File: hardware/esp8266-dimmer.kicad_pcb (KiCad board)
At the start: 2 copper layers, 68.5 x 26 mm, 18 parts, among them J1 Conn_01x06, J2 Conn_01x05, J3 Screw_Terminal_01x02, Q1 PMV16XN, Q2 PMV16XN, Q3 PMV16XN, Q4 PMV16XN, U1 LD1117S33TR_SOT223, U2 ESP-12E

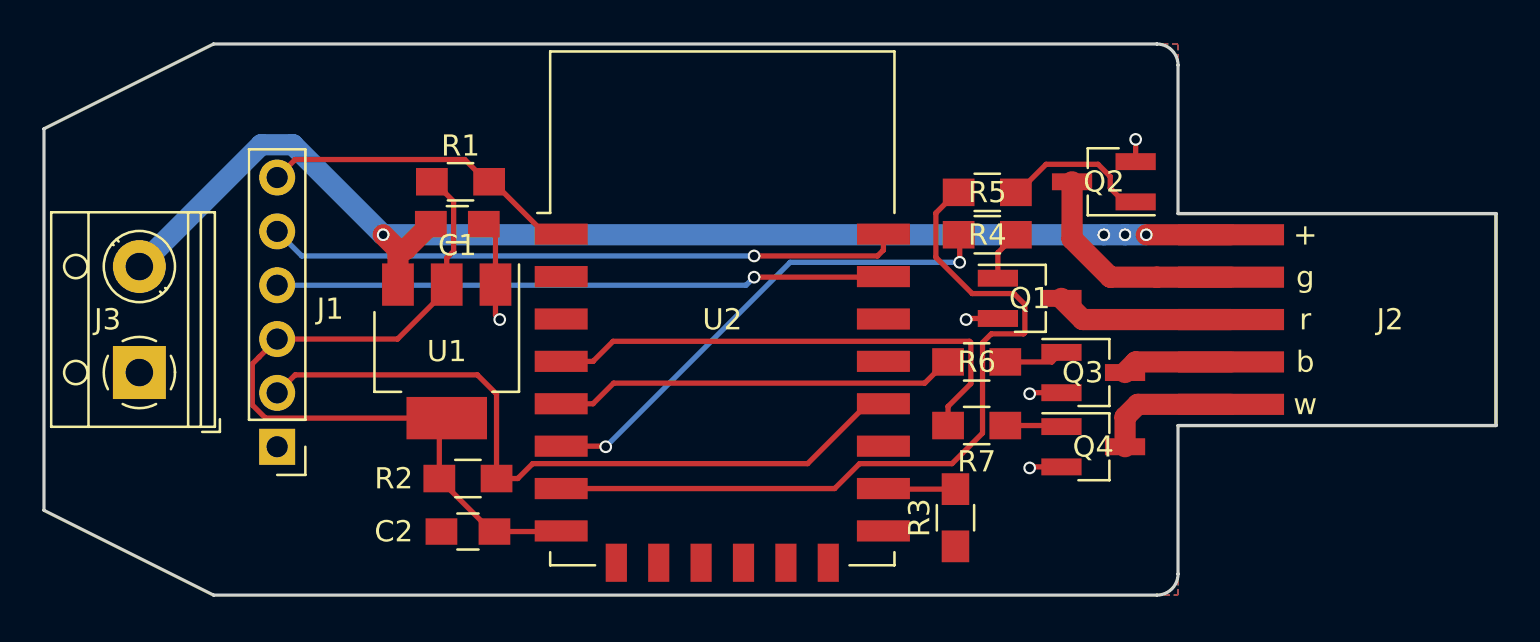
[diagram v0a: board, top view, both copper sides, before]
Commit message: Fix missing ESP-12E ch en pull up resistor + pin use changes + redo the layout
RGBW pins changed a bit to allow nicer layout. Not to mention error fix (pull up
ch en resistor) and all kinds of layout tweaks.
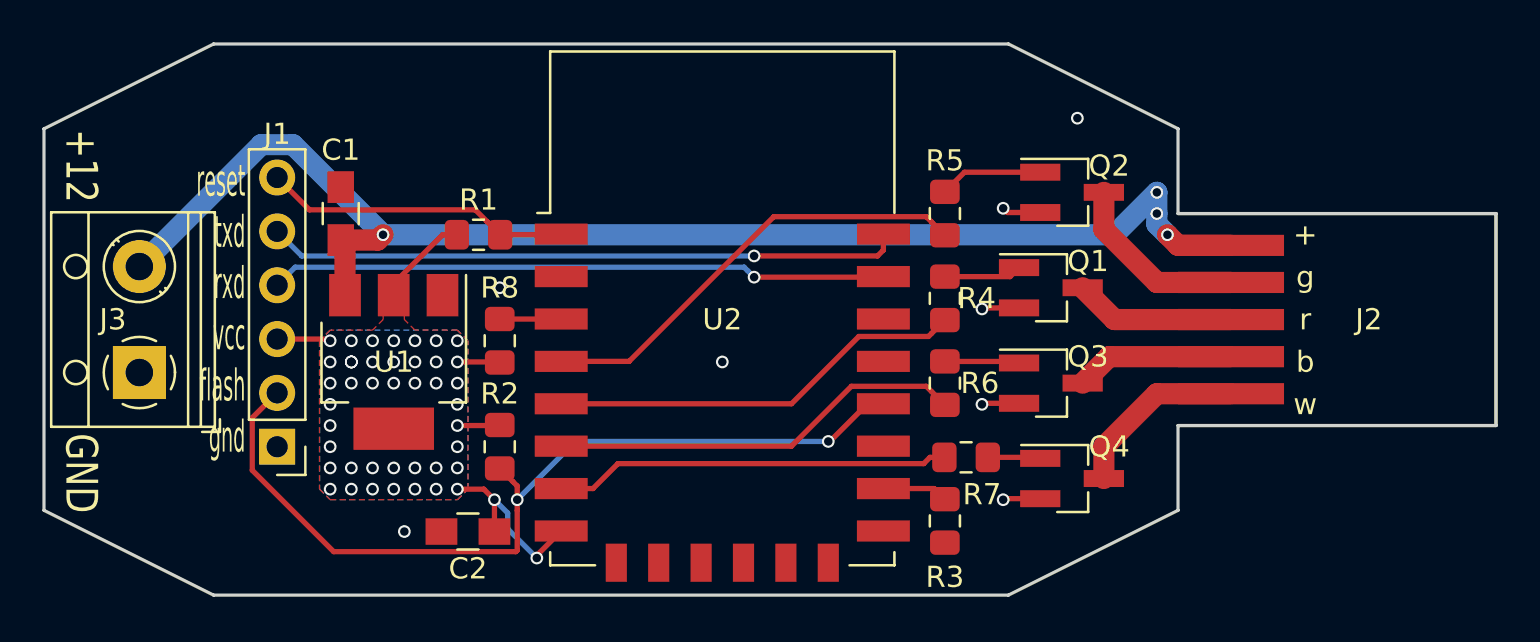
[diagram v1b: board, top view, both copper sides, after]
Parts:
- added R8: 10K, Resistor_SMD:R_0805_2012Metric_Pad1.15x1.40mm_HandSolder, F.Cu at (135.0, 103.0)
- R1, R2, R3, R4, R5, R6, R7: footprint Resistors_SMD:R_0805_HandSoldering -> Resistor_SMD:R_0805_2012Metric_Pad1.15x1.40mm_HandSolder
- moved C1 5.52 mm to (127.5, 97.0), turned to 90 degrees
- moved R4 3.61 mm to (156.0, 101.0), turned to 270 degrees
- moved R1 2.64 mm to (134.0, 98.0)
- moved U1 2.55 mm to (130.0, 104.0)
- moved R5 2.24 mm to (156.0, 97.0), turned to 270 degrees
- moved R2 2.12 mm to (135.0, 108.0), turned to 90 degrees
- moved Q3 2.06 mm to (161.0, 105.0)
- moved Q4 1.80 mm to (162.0, 109.5)
- moved R6 1.80 mm to (156.0, 105.0), turned to 270 degrees
- moved Q2 1.58 mm to (162.0, 96.0), turned to 0 degrees
- moved R7 1.58 mm to (157.0, 108.5)
- moved Q1 1.12 mm to (161.0, 100.5)
- moved R3 0.52 mm to (156.0, 111.5)
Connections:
- U2 pad 3: (no net) -> Net-(R8-Pad1)
- U2 pad 4: W_PWM -> G_PWM
- U2 pad 5: B_PWM -> R_PWM
- U2 pad 6: R_PWM -> B_PWM
- U2 pad 7: G_PWM -> W_PWM
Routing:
- net VCC: track 38.4 -> 20.2 mm, vias 0 -> 45
- net G_PWM: track 37.4 -> 21.3 mm
- net FLASH: track 34.8 -> 41.6 mm, vias 0 -> 2
- net W_PWM: track 24.1 -> 18.7 mm
- net R_PWM: track 23.7 -> 19.7 mm, vias 2 -> 0
- net GND: track 10.4 -> 7.39 mm, vias 5 -> 8
- net Net-(R8-Pad1): track 0.00 -> 2.90 mm
- net +12V: track 60.6 -> 63.2 mm
- net Net-(Q2-Pad1): track 7.26 -> 4.88 mm
- net /PB: track 5.21 -> 7.52 mm
- net /PG: track 10.9 -> 8.79 mm
- net /PW: track 6.65 -> 8.54 mm
- net Net-(Q1-Pad1): track 2.40 -> 3.68 mm
- net /PR: track 8.41 -> 7.62 mm
- net Net-(Q3-Pad1): track 2.84 -> 3.53 mm
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- added copper zone on B.Cu, net VCC
- added copper zone on F.Cu, net VCC
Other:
- outline, holes or cut-outs redrawn
- board text added: "+12"
- board text added: "GND"
- board text added: "pretty lights"
- board text added: "reset txd rxd vcc flash gnd"
